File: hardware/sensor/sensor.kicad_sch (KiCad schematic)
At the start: 32 parts, among them IC1 ATTINY202-SSN, IC2 Si4012-C1001GTR, IC3 TPS3839L30DBZR, J1 M20-9770342

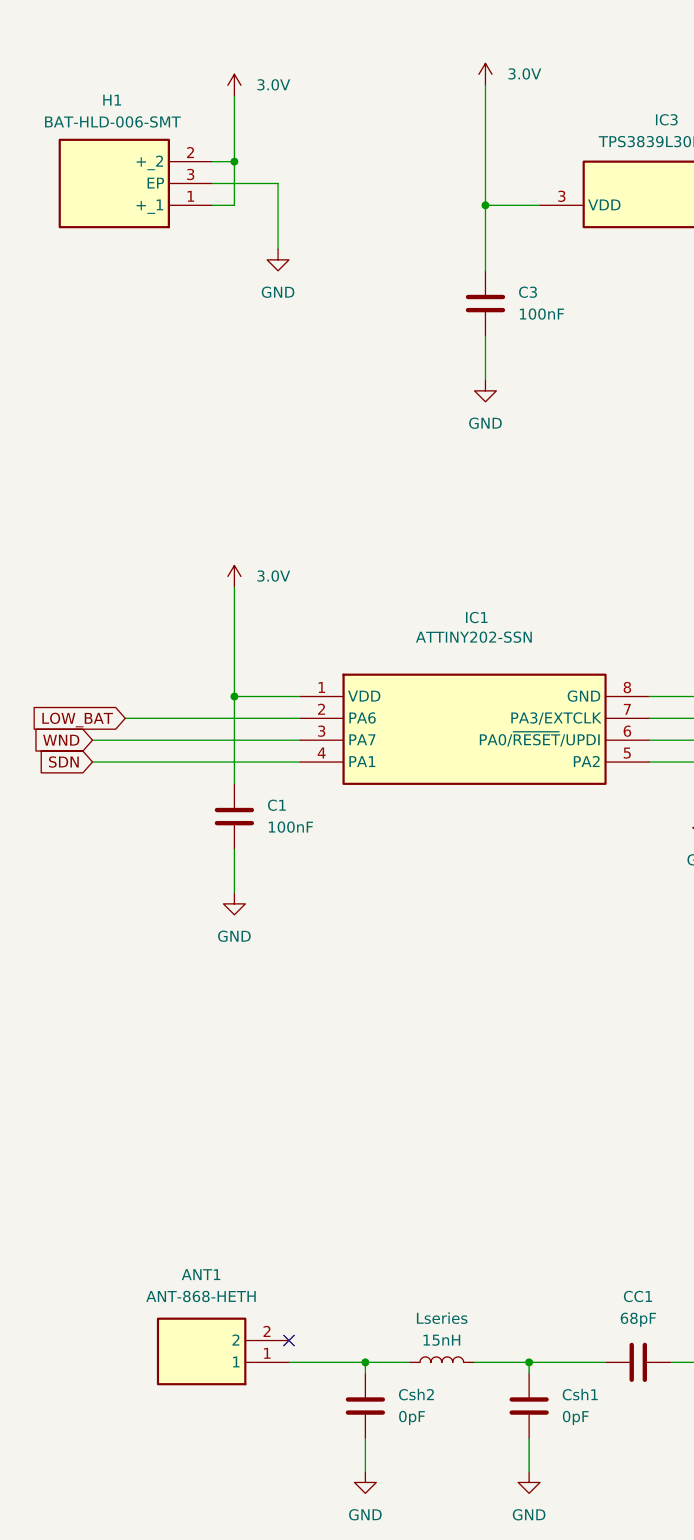
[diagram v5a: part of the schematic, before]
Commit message: EG-21 Schematic complete, without ERC errors. All components updated in the PCB.
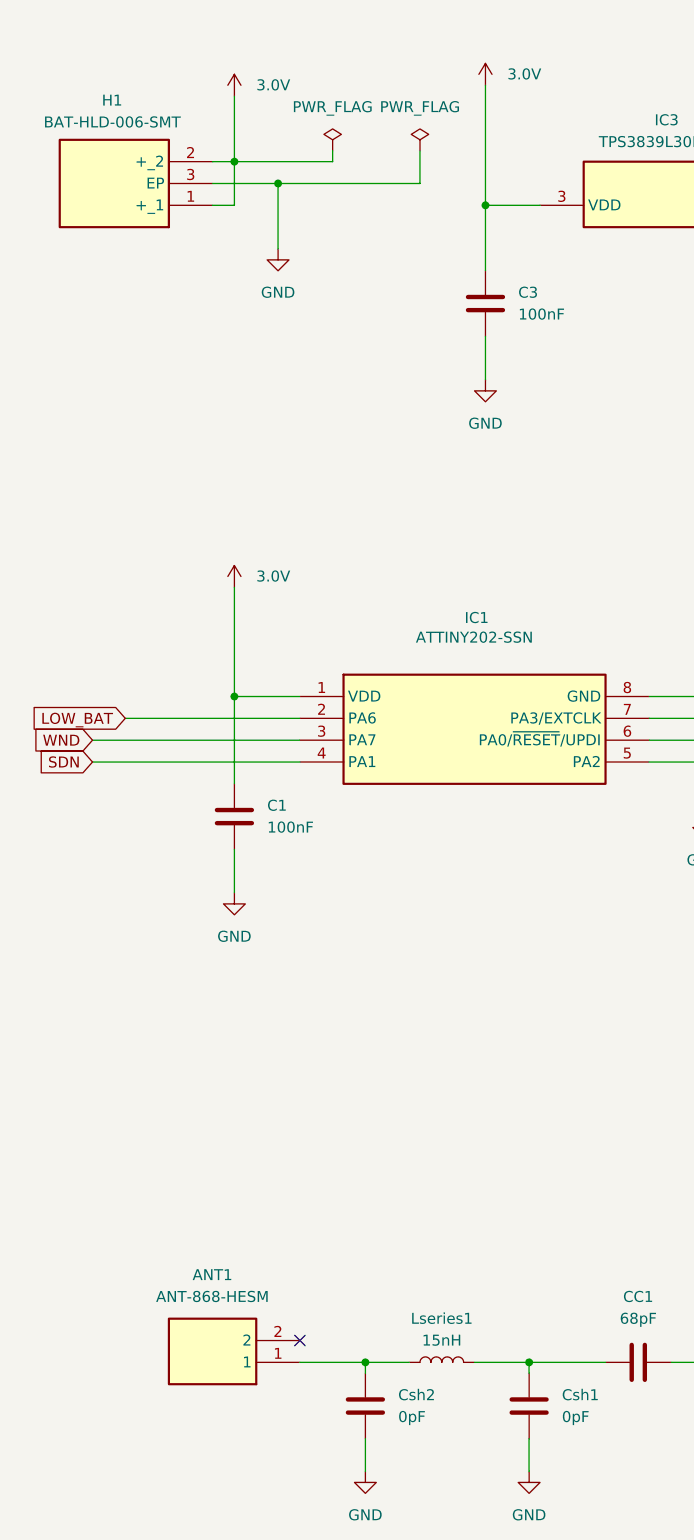
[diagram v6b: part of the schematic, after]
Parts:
- removed ANT1: ANT-868-HETH, MyParts:ANT-868-HESM, symbol ANT-868-HESM:ANT-868-HETH
- added ANT1: ANT-868-HESM, MyParts:ANT-868-HESM, symbol ANT-868-HESM:ANT-868-HESM
- CC1, CM1, CM2, CM3, CM6: footprint Inductor_SMD:L_0402_1005Metric -> Capacitor_SMD:C_0402_1005Metric
- CM5, Csh1, Csh2: footprint (none) -> Capacitor_SMD:C_0402_1005Metric
- R2: footprint (none) -> Resistor_SMD:R_0603_1608Metric
- renumbered Lseries to Lseries1
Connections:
- net at Csh2.1, Lseries1.1: now also ANT1.1

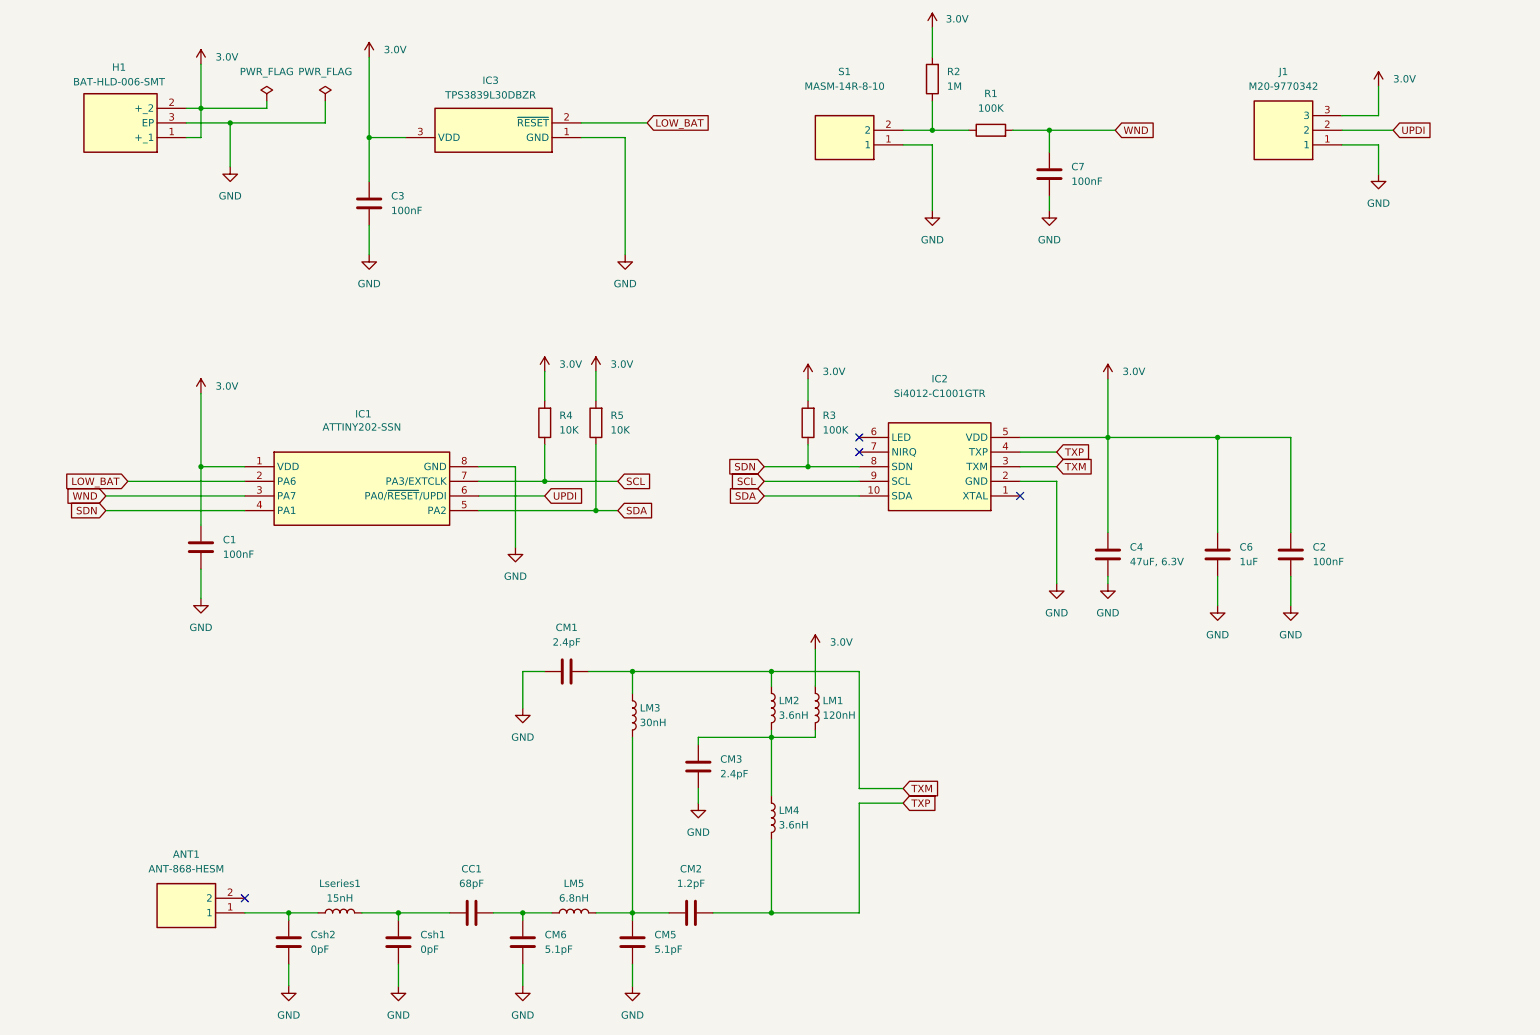
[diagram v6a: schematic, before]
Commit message: EG-21 All components information inserted. BOM generated.
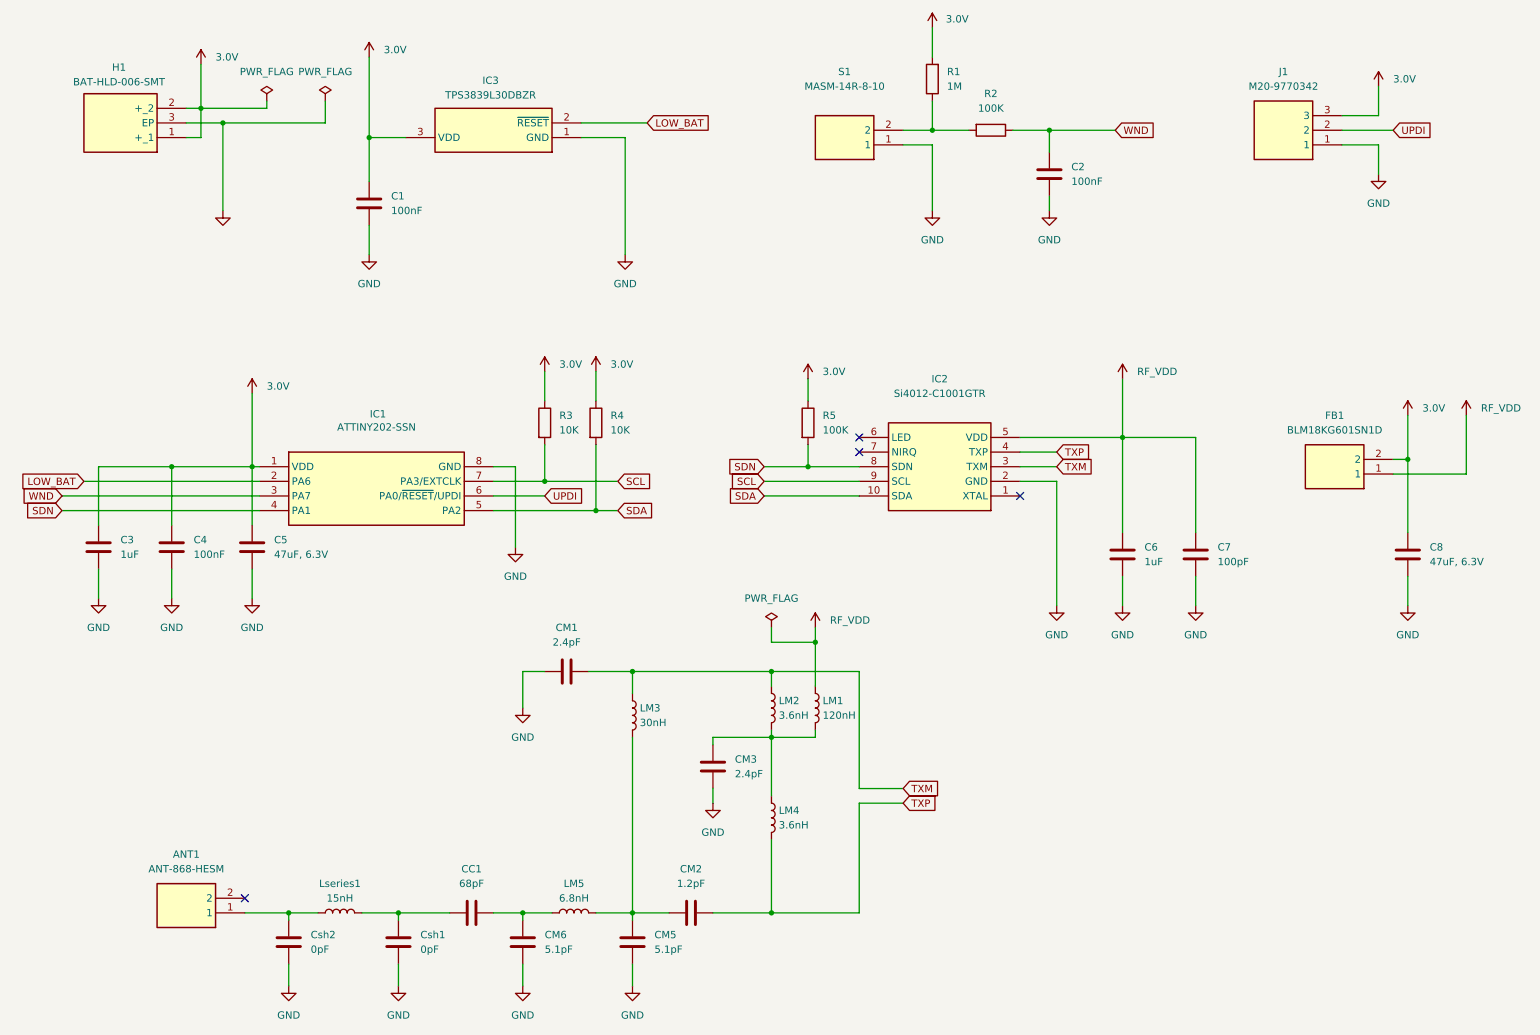
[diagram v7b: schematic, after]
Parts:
- removed C1: 100nF, Capacitor_SMD:C_0603_1608Metric, symbol Device:C
- removed R1: 100K, Resistor_SMD:R_0201_0603Metric, symbol Device:R
- added C3: 1uF, Capacitor_SMD:C_0603_1608Metric, symbol Device:C
- added C5, C8: 47uF, 6.3V, Capacitor_SMD:C_1206_3216Metric, symbol Device:C
- added FB1: BLM18KG601SN1D, MyParts:BLM18SP221SN1B, symbol BLM18KG601SN1D:BLM18KG601SN1D
- added R2: 100K, Resistor_SMD:R_0603_1608Metric, symbol Device:R
- ANT1: Mouser Price/Stock https://eu.mouser.com/ProductDetail/TE-Connectivity-Linx-Te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 -> https://pt.mouser.com/ProductDetail/TE-Connectivity-Linx-Te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
- C1: renamed from C3; Manufacturer_Name (none) -> Murata; Manufacturer_Part_Number (none) -> GCJ188R72A104KA1D; Mouser Part Number (none) -> 81-GCJ188R72A104KA1D; Mouser Price/Stock (none) -> https://pt.mouser.com/ProductDetail/Murata-Electronics/GCJ1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
- C2: Manufacturer_Name (none) -> Murata; Manufacturer_Part_Number (none) -> GCJ188R72A104KA1D; Mouser Part Number (none) -> 81-GCJ188R72A104KA1D; Mouser Price/Stock (none) -> https://pt.mouser.com/ProductDetail/Murata-Electronics/GCJ1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
- C4: value 47uF, 6.3V -> 100nF; footprint Capacitor_SMD:C_0805_2012Metric -> Capacitor_SMD:C_0603_1608Metric; Manufacturer_Name (none) -> Murata; Manufacturer_Part_Number (none) -> GCJ188R72A104KA1D; Mouser Part Number (none) -> 81-GCJ188R72A104KA1D; Mouser Price/Stock (none) -> https://pt.mouser.com/ProductDetail/Murata-Electronics/GCJ1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
- C6: Manufacturer_Name (none) -> TAYO YUDEN; Manufacturer_Part_Number (none) -> MBASE168SB7105KTNA18; Mouser Part Number (none) -> 963-MBASE168SB7105KT; Mouser Price/Stock (none) -> https://pt.mouser.com/ProductDetail/TAIYO-YUDEN/MBASE168SB7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
- C7: value 100nF -> 100pF; Manufacturer_Name (none) -> Vishay; Manufacturer_Part_Number (none) -> VJ0603Y101MXQCW1BC; Mouser Part Number (none) -> 77-VJ0603Y101MXQCBC; Mouser Price/Stock (none) -> https://pt.mouser.com/ProductDetail/Vishay-Vitramon/VJ0603Y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
- CC1: Manufacturer_Name (none) -> Murata; Manufacturer_Part_Number (none) -> GRM1555C1H680FA01J; Mouser Part Number (none) -> 81-GRM1555C1H680FA1J; Mouser Price/Stock (none) -> https://eu.mouser.com/ProductDetail/Murata-Electronics/GRM1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
- CM1, CM3: Manufacturer_Name (none) -> Murata; Manufacturer_Part_Number (none) -> GRM1555C1H2R4WA01D; Mouser Part Number (none) -> 81-GRM1555C1H2R4WA1D; Mouser Price/Stock (none) -> https://eu.mouser.com/ProductDetail/Murata-Electronics/GRM1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
- CM2: Manufacturer_Name (none) -> Murata; Manufacturer_Part_Number (none) -> GRM1555C1H1R2WA01D; Mouser Part Number (none) -> 81-GRM1555C1H1R2WA1D; Mouser Price/Stock (none) -> https://pt.mouser.com/ProductDetail/Murata-Electronics/GRM1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
- CM5, CM6: Manufacturer_Name (none) -> Murata; Manufacturer_Part_Number (none) -> GRM1555C1H5R1WA01D; Mouser Part Number (none) -> 81-GRM1555C1H5R1WA1D; Mouser Price/Stock (none) -> https://eu.mouser.com/ProductDetail/Murata-Electronics/GRM1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
- H1: Mouser Price/Stock https://www.mouser.co.uk/ProductDetail/TE-Connectivity-Linx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 -> https://pt.mouser.com/ProductDetail/TE-Connectivity-Linx-Te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
- IC1: Mouser Price/Stock https://www.mouser.co.uk/ProductDetail/Microchip-Technology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 -> https://pt.mouser.com/ProductDetail/Microchip-Technology/AT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
- IC2: Mouser Price/Stock https://www.mouser.co.uk/ProductDetail/Silicon-Labs/SI4012-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 -> https://pt.mouser.com/ProductDetail/Silicon-Labs/SI4012-C10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
- IC3: Mouser Price/Stock https://www.mouser.co.uk/ProductDetail/Texas-Instruments/TP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 -> https://pt.mouser.com/ProductDetail/Texas-Instruments/TPS38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
- J1: Mouser Price/Stock https://www.mouser.co.uk/ProductDetail/Harwin/M20-9770342?q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 -> https://pt.mouser.com/ProductDetail/Harwin/M20-9770342?qs=J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
- LM1: Manufacturer_Name (none) -> Coilcraft; Manufacturer_Part_Number (none) -> 0603HP-R12XGLU; Mouser Part Number (none) -> 994-0603HP-R12XGLU; Mouser Price/Stock (none) -> https://pt.mouser.com/ProductDetail/Coilcraft/0603HP-R12XGL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
- LM2, LM4: Manufacturer_Name (none) -> Coilcraft; Manufacturer_Part_Number (none) -> 0402HP-3N6XGRW; Mouser Part Number (none) -> 994-0402HP-3N6XGRW; Mouser Price/Stock (none) -> https://eu.mouser.com/ProductDetail/Coilcraft/0402HP-3N6XGR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
- LM3: Manufacturer_Name (none) -> Coilcraft; Manufacturer_Part_Number (none) -> 0402HP-30NXJRW; Mouser Part Number (none) -> 994-0402HP-30NXJRW; Mouser Price/Stock (none) -> https://eu.mouser.com/ProductDetail/Coilcraft/0402HP-30NXJR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
- LM5: Manufacturer_Name (none) -> Coilcraft; Manufacturer_Part_Number (none) -> 0402HP-6N8XGRW; Mouser Part Number (none) -> 994-0402HP-6N8XGRW; Mouser Price/Stock (none) -> https://eu.mouser.com/ProductDetail/Coilcraft/0402HP-6N8XGR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
- Lseries1: Manufacturer_Name (none) -> Coilcraft; Manufacturer_Part_Number (none) -> 0402HP-15NXJRW; Mouser Part Number (none) -> 994-0402HP-15NXJRW; Mouser Price/Stock (none) -> https://eu.mouser.com/ProductDetail/Coilcraft/0402HP-15NXJR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
- R1: renamed from R2; Manufacturer_Name (none) -> Rohm; Manufacturer_Part_Number (none) -> SFR03EZPJ105; Mouser Part Number (none) -> 755-SFR03EZPJ105; Mouser Price/Stock (none) -> https://pt.mouser.com/ProductDetail/ROHM-Semiconductor/SFR0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
- R3: value 100K -> 10K; footprint Resistor_SMD:R_0201_0603Metric -> Resistor_SMD:R_0603_1608Metric; Manufacturer_Name (none) -> Yageo; Manufacturer_Part_Number (none) -> AC0603JR-7W10KL; Mouser Part Number (none) -> 603-AC0603JR-7W10KL; Mouser Price/Stock (none) -> https://pt.mouser.com/ProductDetail/YAGEO/AC0603JR-7W10KL?q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
- R4: footprint Resistor_SMD:R_0201_0603Metric -> Resistor_SMD:R_0603_1608Metric; Manufacturer_Name (none) -> Yageo; Manufacturer_Part_Number (none) -> AC0603JR-7W10KL; Mouser Part Number (none) -> 603-AC0603JR-7W10KL; Mouser Price/Stock (none) -> https://pt.mouser.com/ProductDetail/YAGEO/AC0603JR-7W10KL?q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
- R5: value 10K -> 100K; footprint Resistor_SMD:R_0201_0603Metric -> Resistor_SMD:R_0603_1608Metric; Manufacturer_Name (none) -> Vishay; Manufacturer_Part_Number (none) -> RCA0603100KJNEA; Mouser Part Number (none) -> 71-RCA0603100KJNEA; Mouser Price/Stock (none) -> https://pt.mouser.com/ProductDetail/Vishay-Draloric/RCA0603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
- S1: Mouser Price/Stock https://www.mouser.co.uk/ProductDetail/Littelfuse/MASM-14R-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 -> https://pt.mouser.com/ProductDetail/Littelfuse/MASM-14R-8-1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
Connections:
- net 3.0V: now also R3.1, R4.1, R5.1, C3.1, C5.1, C8.1, FB1.2; no longer C2.1, C6.1, IC2.5 (VDD), LM1.1, R3.2, R4.2, R5.2
- net GND: now also C3.2, C5.2, C8.2
- net SCL: now also R3.2; no longer R4.1
- net SDA: now also R4.2; no longer R5.1
- net SDN: now also R5.2; no longer R3.1
- net WND: now also C2.1, R2.1; no longer C7.1
- net at R1.1, S1.2: now also R2.2
- new net RF_VDD: C6.1, C7.1, FB1.1, IC2.5 (VDD), LM1.1
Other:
- moved on the sheet: IC1

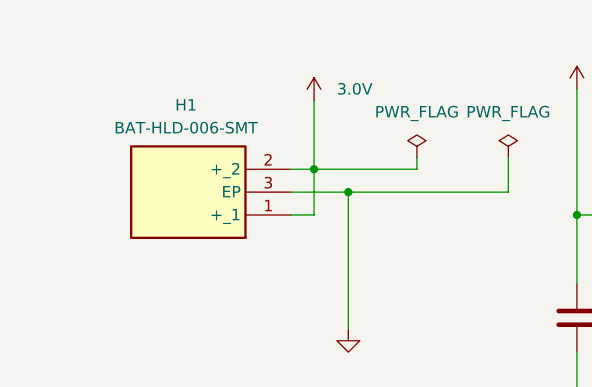
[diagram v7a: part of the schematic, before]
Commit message: EG-22 All components placed, battery counter yard changed. No connections, and not final places for all components.
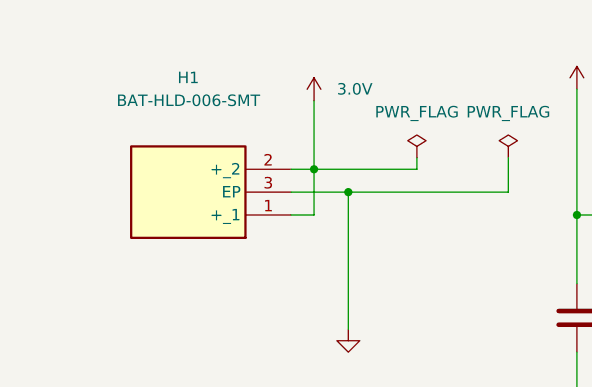
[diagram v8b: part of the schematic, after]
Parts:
- H1: Mouser Price/Stock https://pt.mouser.com/ProductDetail/TE-Connectivity-Linx-Te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 -> https://www.mouser.co.uk/ProductDetail/TE-Connectivity-Linx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
- J1: Mouser Price/Stock https://pt.mouser.com/ProductDetail/Harwin/M20-9770342?qs=J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 -> https://www.mouser.co.uk/ProductDetail/Harwin/M20-9770342?q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
